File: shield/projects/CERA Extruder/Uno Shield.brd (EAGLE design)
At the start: 55.9 x 53.3 mm, 5 parts

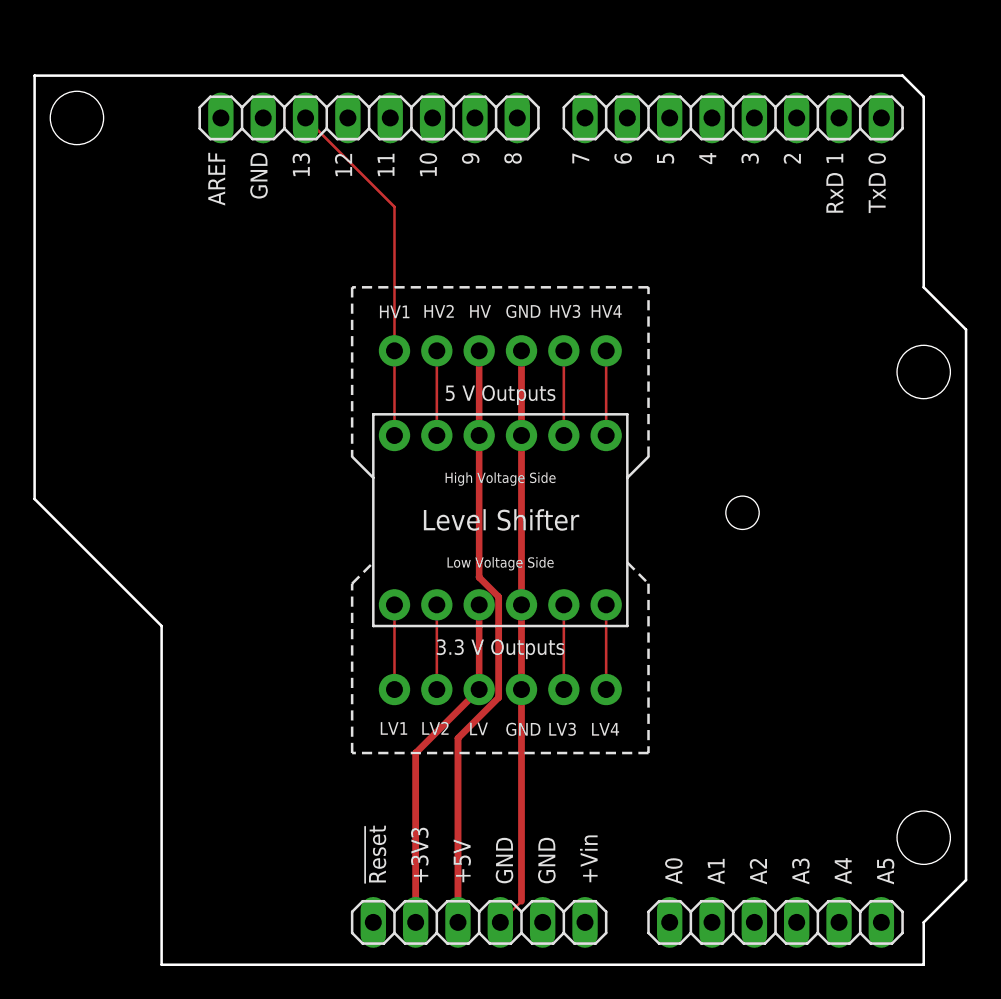
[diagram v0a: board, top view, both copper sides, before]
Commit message: made it so that the Uno board has a more conventional shape
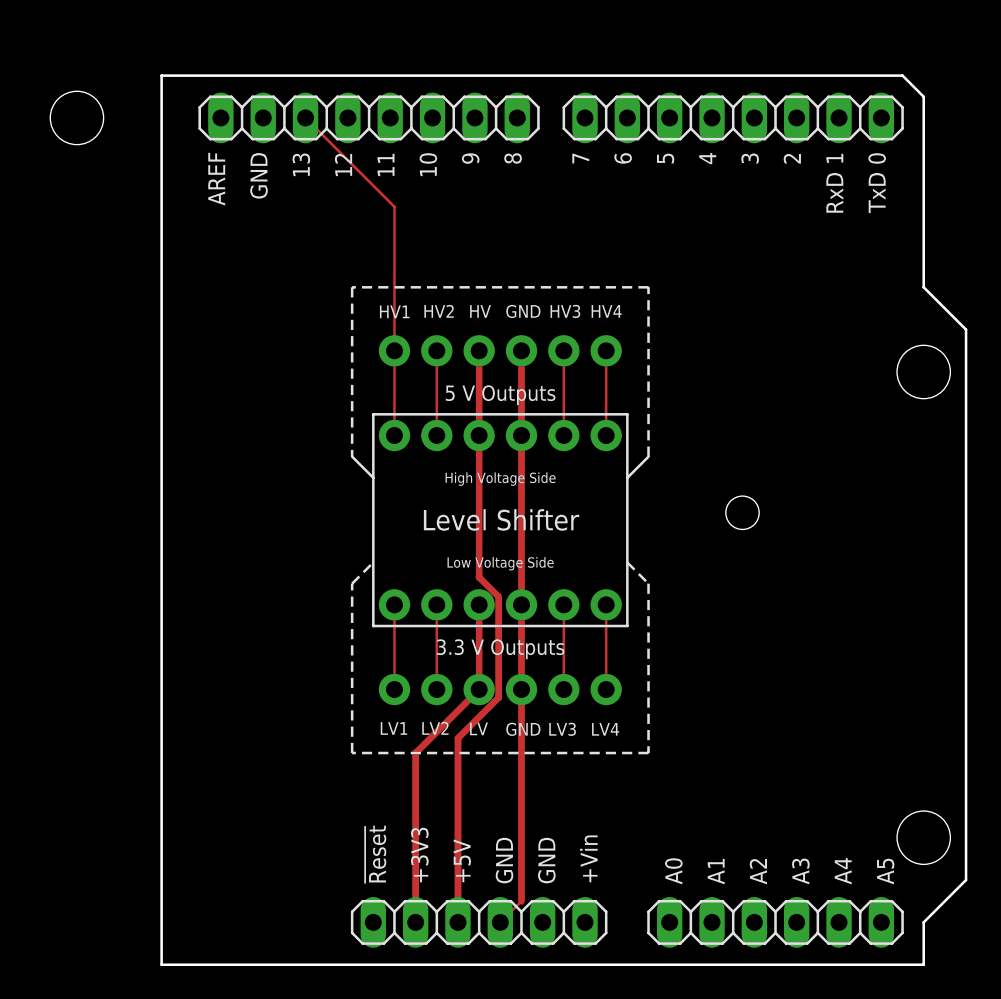
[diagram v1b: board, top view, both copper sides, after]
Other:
- board size 55.9 x 53.3 mm -> 48.3 x 53.3 mm
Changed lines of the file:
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@@
 <drawing>
 <settings>
-<setting alwaysvectorfont="no"/>
+<setting alwaysvectorfont="yes"/>
 <setting verticaltext="up"/>
 </settings>
@@
 <board>
 <plain>
-<wire x1="12.7" y1="53.34" x2="12.7" y2="27.94" width="0.1524" layer="20"/>
-<wire x1="12.7" y1="27.94" x2="20.32" y2="20.32" width="0.1524" layer="20"/>
-<wire x1="20.32" y1="20.32" x2="20.32" y2="0" width="0.1524" layer="20"/>
+<wire x1="64.77" y1="53.34" x2="20.32" y2="53.34" width="0.1524" layer="20"/>
+<wire x1="20.32" y1="53.34" x2="20.32" y2="0" width="0.1524" layer="20"/>
 <wire x1="20.32" y1="0" x2="66.04" y2="0" width="0.1524" layer="20"/>
 <wire x1="66.04" y1="0" x2="66.04" y2="2.54" width="0.1524" layer="20"/>
@@
 <wire x1="66.04" y1="40.64" x2="66.04" y2="52.07" width="0.1524" layer="20"/>
 <wire x1="66.04" y1="52.07" x2="64.77" y2="53.34" width="0.1524" layer="20"/>
-<wire x1="64.77" y1="53.34" x2="12.7" y2="53.34" width="0.1524" layer="20"/>
 <wire x1="31.75" y1="40.64" x2="31.75" y2="30.48" width="0.1524" layer="21" style="shortdash"/>
 <wire x1="31.75" y1="30.48" x2="33.02" y2="29.21" width="0.1524" layer="21"/>

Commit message: updated shields, should be ready for production
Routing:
- net S$5: track 35.8 -> 39.0 mm
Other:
- board text added: "3.3 V Inputs/Outputs"
- board text added: "5 V Inputs/Outputs"
- board text added: "JSLab Distance Sensor Processor"
- board text added: "Made for Arduino Uno Designed in Ithaca, NY by Kevin Guo Design Date: December 2019"
- board text removed: "3.3 V Outputs"
- board text removed: "5 V Outputs"
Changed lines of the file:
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@@
 <text x="40.9448" y="38.8112" size="0.762" layer="21" font="vector" ratio="15">GND</text>
 <text x="38.735" y="38.8112" size="0.762" layer="21" font="vector" ratio="15">HV</text>
-<text x="40.64" y="19.05" size="0.9144" layer="21" align="center">3.3 V Outputs</text>
-<text x="40.64" y="34.29" size="0.9144" layer="21" align="center">5 V Outputs</text>
+<text x="40.64" y="19.05" size="0.9144" layer="21" align="center">3.3 V Inputs/Outputs</text>
+<text x="40.64" y="34.29" size="0.9144" layer="21" align="center">5 V Inputs/Outputs</text>
 <wire x1="33.02" y1="33.02" x2="33.02" y2="20.32" width="0.1524" layer="21"/>
 <wire x1="33.02" y1="20.32" x2="48.26" y2="20.32" width="0.1524" layer="21"/>
@@
 <text x="40.64" y="24.13" size="0.6096" layer="21" font="vector" align="center">Low Voltage Side</text>
 <text x="40.64" y="29.21" size="0.6096" layer="21" font="vector" align="center">High Voltage Side</text>
+<text x="58.42" y="8.89" size="2.1844" layer="25" rot="R90">JSLab
+Distance Sensor Processor</text>
+<text x="63.5" y="8.89" size="1.016" layer="25" rot="R90">Made for Arduino Uno
+Designed in Ithaca, NY by Kevin Guo
+Design Date: December 2019</text>
 </plain>
 <attributes>
@@
 <wire x1="36.83" y1="21.59" x2="37.2482" y2="21.59" width="0.254" layer="16"/>
 <contactref element="JP3" pad="5"/>
-<wire x1="36.83" y1="21.59" x2="36.83" y2="16.51" width="0.1524" layer="1"/>
+<wire x1="36.83" y1="21.59" x2="36.83" y2="16.51" width="0.4064" layer="1"/>
 </signal>
 <signal name="HV4">
@@
 <wire x1="41.91" y1="21.59" x2="41.91" y2="16.51" width="0.4064" layer="1"/>
 <wire x1="41.91" y1="16.51" x2="41.91" y2="3.81" width="0.4064" layer="1"/>
-<wire x1="41.91" y1="3.81" x2="40.64" y2="2.54" width="0.1524" layer="1"/>
-</signal>
-<signal name="S$5">
-<contactref element="JP4" pad="3"/>
-<contactref element="E$1" pad="3"/>
-<contactref element="JP2" pad="3"/>
-<wire x1="38.1" y1="2.54" x2="38.1" y2="13.58763125" width="0.4064" layer="1"/>
-<wire x1="38.1" y1="13.58763125" x2="40.5384" y2="16.02603125" width="0.4064" layer="1"/>
-<wire x1="40.5384" y1="16.02603125" x2="40.5384" y2="22.07396875" width="0.4064" layer="1"/>
-<wire x1="39.37" y1="23.24236875" x2="39.37" y2="31.75" width="0.4064" layer="1"/>
-<wire x1="40.5384" y1="22.07396875" x2="39.37" y2="23.24236875" width="0.4064" layer="1"/>
-<wire x1="39.37" y1="36.83" x2="39.37" y2="31.75" width="0.4064" layer="1"/>
+<wire x1="41.91" y1="3.81" x2="40.64" y2="2.54" width="0.4064" layer="1"/>
 </signal>
 <signal name="S$2">
@@
 <contactref element="E$1" pad="26"/>
 <contactref element="JP2" pad="1"/>
-<wire x1="28.956" y1="50.8" x2="34.29" y2="45.466" width="0.1524" layer="1"/>
-<wire x1="34.29" y1="45.466" x2="34.29" y2="36.83" width="0.1524" layer="1"/>
-<wire x1="34.29" y1="36.83" x2="34.29" y2="31.75" width="0.1524" layer="1"/>
+<wire x1="28.956" y1="50.8" x2="34.29" y2="45.466" width="0.4064" layer="1"/>
+<wire x1="34.29" y1="45.466" x2="34.29" y2="36.83" width="0.4064" layer="1"/>
+<wire x1="34.29" y1="36.83" x2="34.29" y2="31.75" width="0.4064" layer="1"/>
 </signal>
 <signal name="S$3">
 <contactref element="JP2" pad="2"/>
 <contactref element="JP4" pad="2"/>
-<wire x1="36.83" y1="36.83" x2="36.83" y2="31.75" width="0.1524" layer="1"/>
+<wire x1="36.83" y1="36.83" x2="36.83" y2="31.75" width="0.4064" layer="1"/>
 </signal>
 <signal name="S$6">
 <contactref element="JP2" pad="5"/>
 <contactref element="JP4" pad="5"/>
-<wire x1="44.45" y1="36.83" x2="44.45" y2="31.75" width="0.1524" layer="1"/>
+<wire x1="44.45" y1="36.83" x2="44.45" y2="31.75" width="0.4064" layer="1"/>
 </signal>
 <signal name="S$7">
 <contactref element="JP2" pad="6"/>
 <contactref element="JP4" pad="6"/>
-<wire x1="46.99" y1="36.83" x2="46.99" y2="31.75" width="0.1524" layer="1"/>
+<wire x1="46.99" y1="36.83" x2="46.99" y2="31.75" width="0.4064" layer="1"/>
 </signal>
 <signal name="S$8">
 <contactref element="JP3" pad="1"/>
 <contactref element="JP1" pad="1"/>
-<wire x1="46.99" y1="21.59" x2="46.99" y2="16.51" width="0.1524" layer="1"/>
+<wire x1="46.99" y1="21.59" x2="46.99" y2="16.51" width="0.4064" layer="1"/>
 </signal>
 <signal name="S$9">
 <contactref element="JP3" pad="2"/>
 <contactref element="JP1" pad="2"/>
-<wire x1="44.45" y1="21.59" x2="44.45" y2="16.51" width="0.1524" layer="1"/>
+<wire x1="44.45" y1="21.59" x2="44.45" y2="16.51" width="0.4064" layer="1"/>
 </signal>
 <signal name="S$10">
 <contactref element="JP3" pad="6"/>
 <contactref element="JP1" pad="6"/>
-<wire x1="34.29" y1="21.59" x2="34.29" y2="16.51" width="0.1524" layer="1"/>
+<wire x1="34.29" y1="21.59" x2="34.29" y2="16.51" width="0.4064" layer="1"/>
+</signal>
+<signal name="S$5">
+<contactref element="JP2" pad="3"/>
+<contactref element="E$1" pad="3"/>
+<contactref element="JP4" pad="3"/>
+<wire x1="39.37" y1="36.83" x2="39.37" y2="31.75" width="0.4064" layer="16"/>
+<wire x1="39.37" y1="31.75" x2="39.37" y2="28.501975" width="0.4064" layer="16"/>
+<wire x1="38.1" y1="10.868025" x2="38.1" y2="2.54" width="0.4064" layer="16"/>
+<wire x1="39.37" y1="28.501975" x2="32.9946" y2="22.126575" width="0.4064" layer="16"/>
+<wire x1="32.9946" y1="15.973425" x2="38.1" y2="10.868025" width="0.4064" layer="16"/>
+<wire x1="32.9946" y1="22.126575" x2="32.9946" y2="15.973425" width="0.4064" layer="16"/>
 </signal>
 </signals>
@@
 </board>
 </drawing>
+<compatibility>
+<note version="6.3" minversion="6.2.2" severity="warning">
+Since Version 6.2.2 text objects can contain more than one line,
+which will not be processed correctly with this version.
+</note>
+</compatibility>
 </eagle>
